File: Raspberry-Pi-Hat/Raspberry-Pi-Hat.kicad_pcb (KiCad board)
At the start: 4 copper layers, 65 x 56 mm, 129 parts, among them J1 Screw_Terminal_01x04, J10 Conn_01x03, J2 Screw_Terminal_01x02, J3 40HAT, J4 Screw_Terminal_01x02, J5 USB_B, J6 Conn_01x03, J7 USB_A, J8 USB_A, J9 CONN_01X02, Q1 DMG2305UX, Q2 DMMT5401, U1 ADM3490ExR, U11 TLV71211_SOT23-5, U2 CAT24C32, U3 TCAN330, U4 LMZ13608, U5 TUSB4041I, U6 MCP2221AxSL, U7 MCP2221AxSL, U8 TPS2561, U9 TPS2561, Y1 24MHz

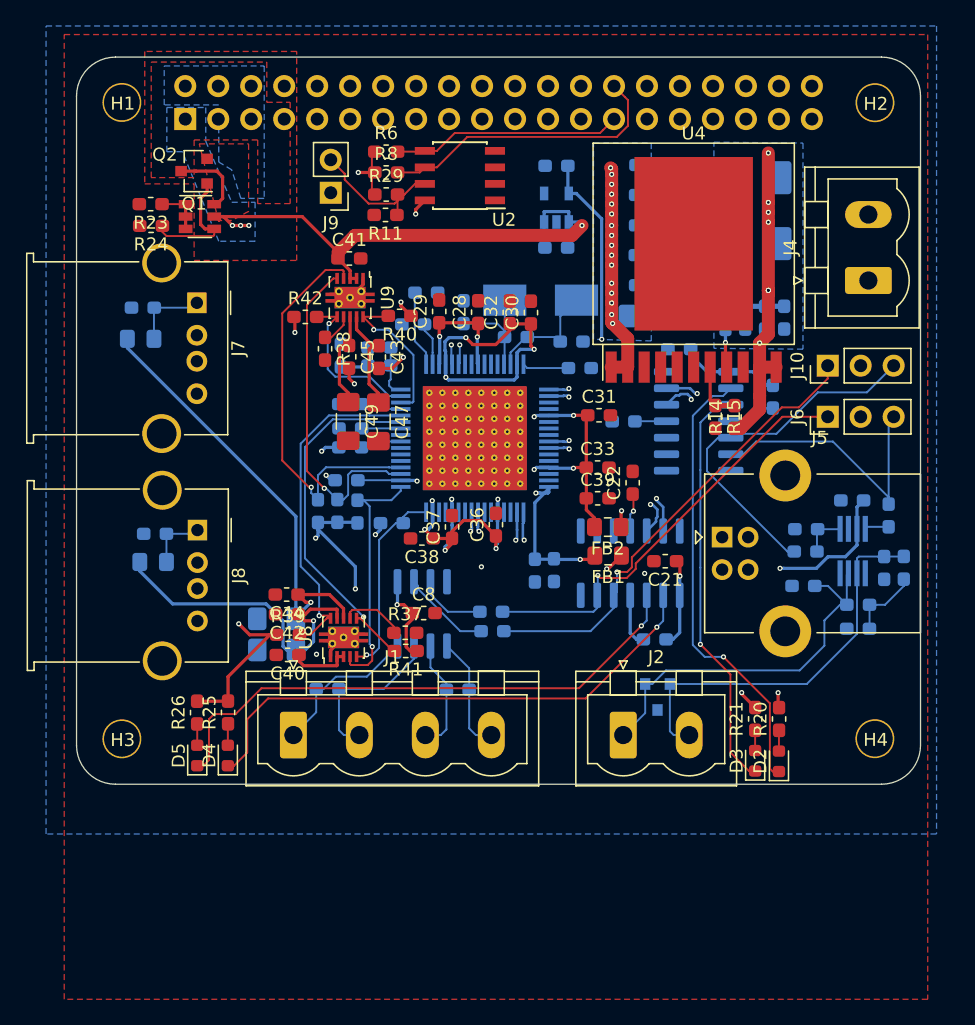
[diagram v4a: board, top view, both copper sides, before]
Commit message: Routing version SPI V0
Replaced USB with SPI for N2K
Power button
RTC

Routing done
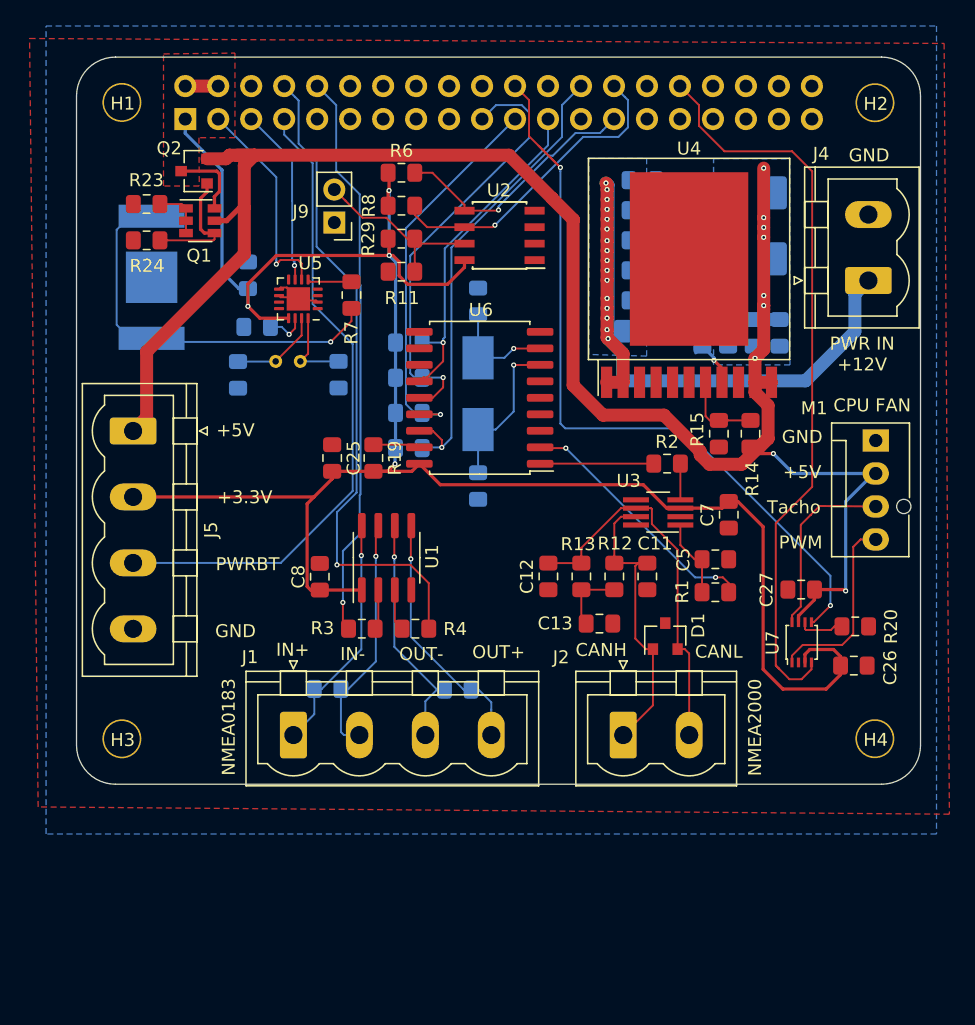
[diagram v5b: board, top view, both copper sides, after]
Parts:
- removed C28, C29, C30, C31, C32, C33, C34, C36, C37, C38, C40, C41, C42, C43, C44, C45, C50, C51: 100nF, Capacitor_SMD:C_0603_1608Metric_Pad1.05x0.95mm_HandSolder
- removed C35, C39: 10uF, Capacitor_SMD:C_0603_1608Metric_Pad1.05x0.95mm_HandSolder
- removed C46, C47, C48, C49: 150uF, Capacitor_SMD:C_1206_3216Metric_Pad1.42x1.75mm_HandSolder
- removed C54, C55: 1uF, Capacitor_SMD:C_0603_1608Metric_Pad1.05x0.95mm_HandSolder
- removed D2, D3, D4, D5: LED, LED_SMD:LED_0603_1608Metric
- removed FB1, FB2: 220 @ 100MHz, Resistor_SMD:R_0805_2012Metric_Pad1.15x1.40mm_HandSolder
- removed FB3, FB4: 200 @ 100MHz, Resistor_SMD:R_0805_2012Metric_Pad1.15x1.40mm_HandSolder
- removed J10, J6: Conn_01x03, Connector_PinHeader_2.54mm:PinHeader_1x03_P2.54mm_Vertical
- removed J7, J8: USB_A, Connector_USB:USB_A_Molex_67643_Horizontal
- removed R21, R25, R26: R_small, Resistor_SMD:R_0603_1608Metric_Pad1.05x0.95mm_HandSolder
- removed R22: 5k, Resistor_SMD:R_0603_1608Metric_Pad1.05x0.95mm_HandSolder
- removed R27, R30, R31, R32, R33, R34, R35, R36: 4.7k, Resistor_SMD:R_0603_1608Metric_Pad1.05x0.95mm_HandSolder
- removed R28: 1M, Resistor_SMD:R_0603_1608Metric_Pad1.05x0.95mm_HandSolder
- removed R37, R38: 25.5k, Resistor_SMD:R_0603_1608Metric_Pad1.05x0.95mm_HandSolder
- removed R39, R40, R41, R42: 10k, Resistor_SMD:R_0603_1608Metric_Pad1.05x0.95mm_HandSolder
- removed U11: TLV71211_SOT23-5, Package_TO_SOT_SMD:SOT-23-5
- removed U8, U9: TPS2561, Package_SON:VSON-10-1EP_3x3mm_P0.5mm_EP1.65x2.4mm_ThermalVias
- added BT1: Battery_Cell, Battery:BatteryHolder_Keystone_2998_1x6.8mm, B.Cu at (84.3, 77.8)
- added M1: Fan_Tacho_PWM, Connector:FanPinHeader_1x04_P2.54mm_Vertical, F.Cu at (140.1, 90.3)
- added R7: TBD, Resistor_SMD:R_0805_2012Metric_Pad1.15x1.40mm_HandSolder, F.Cu at (99.7, 79.1)
- added R9: NC, Resistor_SMD:R_0805_2012Metric_Pad1.15x1.40mm_HandSolder, B.Cu at (104.1, 82.8)
- added Y2: 8MHz, Crystal:Crystal_SMD_Abracon_ABM3-2Pin_5.0x3.2mm_HandSoldering, B.Cu at (109.5, 86.7)
- C10, C16, C17, C18, C2, C3, C4, C6, C8, C9: footprint Capacitor_SMD:C_0603_1608Metric_Pad1.05x0.95mm_HandSolder -> Capacitor_SMD:C_0805_2012Metric_Pad1.15x1.40mm_HandSolder
- C11, C12, C13, C27, C5, C7: footprint Capacitor_SMD:C_0603_1608Metric_Pad1.05x0.95mm_HandSolder -> Capacitor_SMD:C_0805_2012Metric_Pad1.15x1.40mm_HandSolder; moved to F.Cu
- C19: value C -> 47pF; footprint Capacitor_SMD:C_0603_1608Metric_Pad1.05x0.95mm_HandSolder -> Capacitor_SMD:C_0805_2012Metric_Pad1.15x1.40mm_HandSolder
- C20: value C -> 100nF; footprint Capacitor_SMD:C_0603_1608Metric_Pad1.05x0.95mm_HandSolder -> Capacitor_SMD:C_0805_2012Metric_Pad1.15x1.40mm_HandSolder
- C21, C22: value C -> nc; footprint Capacitor_SMD:C_0603_1608Metric_Pad1.05x0.95mm_HandSolder -> Capacitor_SMD:C_0805_2012Metric_Pad1.15x1.40mm_HandSolder; moved to B.Cu
- C23, C24: value 18pF -> 30pF; footprint Capacitor_SMD:C_0603_1608Metric_Pad1.05x0.95mm_HandSolder -> Capacitor_SMD:C_0805_2012Metric_Pad1.15x1.40mm_HandSolder
- C25: value 1uF -> 100nF; footprint Capacitor_SMD:C_0603_1608Metric_Pad1.05x0.95mm_HandSolder -> Capacitor_SMD:C_0805_2012Metric_Pad1.15x1.40mm_HandSolder; moved to F.Cu
- C26: value 10uF -> 100nF; footprint Capacitor_SMD:C_0603_1608Metric_Pad1.05x0.95mm_HandSolder -> Capacitor_SMD:C_0805_2012Metric_Pad1.15x1.40mm_HandSolder; moved to F.Cu
- D1, U1, U3: moved to F.Cu
- J5: value USB_B -> Screw_Terminal_01x04; footprint Connector_USB:USB_B_Lumberg_2411_02_Horizontal -> Connector_Phoenix_MSTB:PhoenixContact_MSTBVA_2,5_4-G-5,08_1x04_P5.08mm_Vertical
- R1, R12, R13, R2, R3, R4: footprint Resistor_SMD:R_0603_1608Metric_Pad1.05x0.95mm_HandSolder -> Resistor_SMD:R_0805_2012Metric_Pad1.15x1.40mm_HandSolder; moved to F.Cu
- R10, R11, R14, R15, R16, R23, R24, R29, R5, R6, R8: footprint Resistor_SMD:R_0603_1608Metric_Pad1.05x0.95mm_HandSolder -> Resistor_SMD:R_0805_2012Metric_Pad1.15x1.40mm_HandSolder
- R17: value 9.53k -> 10k; footprint Resistor_SMD:R_0603_1608Metric_Pad1.05x0.95mm_HandSolder -> Resistor_SMD:R_0805_2012Metric_Pad1.15x1.40mm_HandSolder
- R18: value 90.9k -> 10k; footprint Resistor_SMD:R_0603_1608Metric_Pad1.05x0.95mm_HandSolder -> Resistor_SMD:R_0805_2012Metric_Pad1.15x1.40mm_HandSolder
- R19: value 5k -> 10k; footprint Resistor_SMD:R_0603_1608Metric_Pad1.05x0.95mm_HandSolder -> Resistor_SMD:R_0805_2012Metric_Pad1.15x1.40mm_HandSolder; moved to F.Cu
- R20: value R_small -> 1k; footprint Resistor_SMD:R_0603_1608Metric_Pad1.05x0.95mm_HandSolder -> Resistor_SMD:R_0805_2012Metric_Pad1.15x1.40mm_HandSolder
- U5: value TUSB4041I -> AB0805; footprint Package_QFP:HTQFP-64-1EP_10x10mm_P0.5mm_EP8x8mm_Mask4.4x4.4mm_ThermalVias -> Package_DFN_QFN:VQFN-16-1EP_3x3mm_P0.5mm_EP1.8x1.8mm; moved to F.Cu
- U6: value MCP2221AxSL -> MCP2515-xSO; footprint Package_SO:SOIC-14_3.9x8.7mm_P1.27mm -> Package_SO:SOIC-18W_7.5x11.6mm_P1.27mm; moved to F.Cu
- U7: value MCP2221AxSL -> TXB0102DCU; footprint Package_SO:SOIC-14_3.9x8.7mm_P1.27mm -> Package_SO:VSSOP-8_2.4x2.1mm_P0.5mm; moved to F.Cu
- Y1: value 24MHz -> 32.768 kHz; footprint Crystal:Crystal_SMD_Abracon_ABM3-2Pin_5.0x3.2mm_HandSoldering -> Crystal:Crystal_C26-LF_D2.1mm_L6.5mm_Horizontal
- moved C26 46.2 mm to (138.4, 107.7), turned to 180 degrees
- moved J5 46.1 mm to (82.9, 89.6), turned to 270 degrees
- moved C27 36.0 mm to (134.4, 101.8)
- moved C19 32.6 mm to (92.5, 81.6)
- moved C22 31.5 mm to (91.0, 85.3)
- moved R19 31.1 mm to (101.4, 91.7), turned to 270 degrees
- moved C20 31.0 mm to (91.7, 77.6), turned to 270 degrees
- moved C21 29.0 mm to (98.7, 85.3), turned to 90 degrees
- moved C12 25.9 mm to (114.9, 100.8)
- moved R13 24.8 mm to (117.4, 100.8)
- moved C13 19.9 mm to (118.8, 104.4), turned to 180 degrees
- moved Y1 19.1 mm to (95.8, 84.3)
- moved R12 18.9 mm to (120.0, 100.8), turned to 90 degrees
- moved R2 17.5 mm to (124.0, 92.1), turned to 180 degrees
- moved U5 17.3 mm to (95.6, 79.4), turned to 180 degrees
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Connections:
- C19 pad 1: USB_1_VBUS -> Net-(C19-Pad1)
- C20 pad 1: Net-(C20-Pad1) -> GND
- C20 pad 2: GND -> +3V3
- C21 pad 1: USB_2_VBUS -> GND
- C21 pad 2: GND -> Net-(C21-Pad2)
- C22 pad 1: Net-(C22-Pad1) -> GND
- C22 pad 2: GND -> Net-(C22-Pad2)
- C23 pad 1: GND -> Net-(C23-Pad1)
- C23 pad 2: Net-(C23-Pad2) -> GND
- C24 pad 1: GND -> Net-(C24-Pad1)
- C24 pad 2: Net-(C24-Pad2) -> GND
- C25 pad 2: Net-(C25-Pad2) -> +3V3
- C26 pad 2: /USB-hub/VBUS -> +3V3
- C27 pad 1: Net-(C27-Pad1) -> +5V
- J3 pad 10: /RXD(GPIO15) -> TX_NMEA183
- J3 pad 19: (no net) -> /SPI-MOSI-(GPIO10)
- J3 pad 21: (no net) -> /SPI-MISO-(GPIO9)
- J3 pad 22: (no net) -> /FAN-RPM-(GPIO24)
- J3 pad 23: (no net) -> /SPI-CLK-(GPIO11)
- J3 pad 26: (no net) -> /SPI-CS-(GPIO8)
- J3 pad 3: (no net) -> /I2C-SDA-(GPIO2)
- J3 pad 32: (no net) -> /FAN-PWM-(GPIO12)
- J3 pad 5: (no net) -> /I2C-SCL-(GPIO3)
- J3 pad 7: (no net) -> /Power-Button-(GPIO4)
- J3 pad 8: /TXD(GPIO14) -> RX_NMEA183
- J5 pad 1: /USB-hub/VBUS -> +5V
- J5 pad 2: /USB-hub/USB_UP_N -> +3V3
- J5 pad 3: /USB-hub/USB_UP_P -> /Power-Button-(GPIO4)
- R16 pad 1: Net-(R16-Pad1) -> /SPI-CS-(GPIO8)
- R16 pad 2: GND -> +3V3
- R17 pad 1: Net-(R17-Pad1) -> /SPI-MISO-(GPIO9)
- R17 pad 2: GND -> +3V3
- R18 pad 1: /USB-hub/VBUS -> /SPI-MOSI-(GPIO10)
- R18 pad 2: Net-(R16-Pad1) -> +3V3
- R19 pad 2: USB_1_VBUS -> +3V3
- R20 pad 1: Net-(D2-Pad2) -> GND
- R20 pad 2: +3V3 -> Net-(R20-Pad2)
- U5 pad 1: PWRCTL3 -> (no net)
- U5 pad 10: Net-(R30-Pad1) -> GND
- U5 pad 11: OVERCUR4 -> (no net)
- U5 pad 12: OVERCUR3 -> (no net)
- U5 pad 13: Net-(R31-Pad1) -> +3V3
- U5 pad 14: OVERCUR1 -> Net-(C19-Pad1)
- U5 pad 15: OVERCUR2 -> Net-(C22-Pad2)
- U5 pad 16: Net-(R16-Pad1) -> Net-(C21-Pad2)
- U5 pad 17: Net-(R32-Pad1) -> GND
- U5 pad 2: Net-(C27-Pad1) -> GND
- U5 pad 3: PWRCTL2 -> (no net)
- U5 pad 4: PWRCTL1 -> (no net)
- U5 pad 5: (no net) -> Net-(R7-Pad2)
- U5 pad 6: (no net) -> /I2C-SDA-(GPIO2)
- U5 pad 7: (no net) -> /I2C-SCL-(GPIO3)
- U5 pad 8: Net-(R27-Pad1) -> (no net)
- U5 pad 9: (no net) -> GND
- U6 pad 1: USB_1_VBUS -> RX_CAN
- U6 pad 11: Net-(C20-Pad1) -> (no net)
- U6 pad 12: USB_1_N -> (no net)
- U6 pad 13: USB_1_P -> /SPI-CLK-(GPIO11)
- U6 pad 14: GND -> /SPI-MOSI-(GPIO10)
- U6 pad 2: Net-(D2-Pad1) -> TX_CAN
- U6 pad 3: Net-(D3-Pad1) -> (no net)
- U6 pad 4: Net-(R19-Pad1) -> (no net)
- U6 pad 5: TX_CAN -> (no net)
- U6 pad 6: RX_CAN -> (no net)
- U6 pad 7: (no net) -> Net-(C23-Pad1)
- U6 pad 8: (no net) -> Net-(C24-Pad1)
- U6 pad 9: (no net) -> GND
- U7 pad 1: USB_2_VBUS -> Net-(M1-Pad4)
- U7 pad 2: Net-(D4-Pad1) -> GND
- U7 pad 3: Net-(D5-Pad1) -> +3V3
- U7 pad 4: Net-(R22-Pad1) -> /FAN-PWM-(GPIO12)
- U7 pad 5: TX_NMEA183 -> /FAN-RPM-(GPIO24)
- U7 pad 6: RX_NMEA183 -> Net-(R20-Pad2)
- U7 pad 7: (no net) -> +5V
- U7 pad 8: (no net) -> Net-(M1-Pad3)
- Y1 pad 1: Net-(C23-Pad2) -> Net-(C21-Pad2)
- Y1 pad 2: Net-(C24-Pad2) -> Net-(C22-Pad2)
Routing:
- net Net-(C28-Pad1): track 73.1 -> 0.00 mm, vias 12 -> 0
- net /FAN-RPM-(GPIO24): track 0.00 -> 59.5 mm, vias 0 -> 2
- net /TXD(GPIO14): track 59.3 -> 0.00 mm
- net Net-(C27-Pad1): track 58.0 -> 0.00 mm, vias 6 -> 0
- net /RXD(GPIO15): track 57.9 -> 0.00 mm
- net /FAN-PWM-(GPIO12): track 0.00 -> 57.4 mm
- net /Power-Button-(GPIO4): track 0.00 -> 50.0 mm
- net /USB-hub/USB_UP_P: track 44.2 -> 0.00 mm, vias 1 -> 0
- net /USB-hub/USB_UP_N: track 44.2 -> 0.00 mm, vias 1 -> 0
- net +1V1: track 43.1 -> 0.00 mm, vias 2 -> 0
- net Net-(D5-Pad1): track 43.0 -> 0.00 mm, vias 1 -> 0
- net Net-(D4-Pad1): track 41.6 -> 0.00 mm, vias 1 -> 0
- net /USB-hub/USB_4_P: track 38.5 -> 0.00 mm, vias 1 -> 0
- net /USB-hub/USB_4_N: track 38.5 -> 0.00 mm, vias 1 -> 0
- net +5V: track 103.5 -> 141.9 mm, vias 11 -> 9
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- removed copper zone on B.Cu, net +3V3
- removed copper zone on F.Cu, net +5V
- removed copper zone on B.Cu, net /P5V
- removed copper zone on In2.Cu, net GND
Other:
- copper layers 4 -> 2
- net class Power: trace_width 0.3 -> 0.25
- board text added: "+3.3V"
- board text added: "+5V"
- board text added: "CANH"
- board text added: "CANL"
- board text added: "CPU FAN"
- board text added: "GND"
- board text added: "IN+"
- board text added: "IN-"
- board text added: "NMEA0183"
- board text added: "NMEA2000"
- board text added: "OUT+"
- board text added: "OUT-"
- board text added: "PWM"
- board text added: "PWR IN +12V"
- board text added: "PWRBT"
- board text added: "Tacho"
